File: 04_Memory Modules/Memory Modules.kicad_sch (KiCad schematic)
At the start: 5 parts, among them J1 Data bus, J2 Address bus 1, J3 Address bus 2, J4 Input 1, J5 Input 2

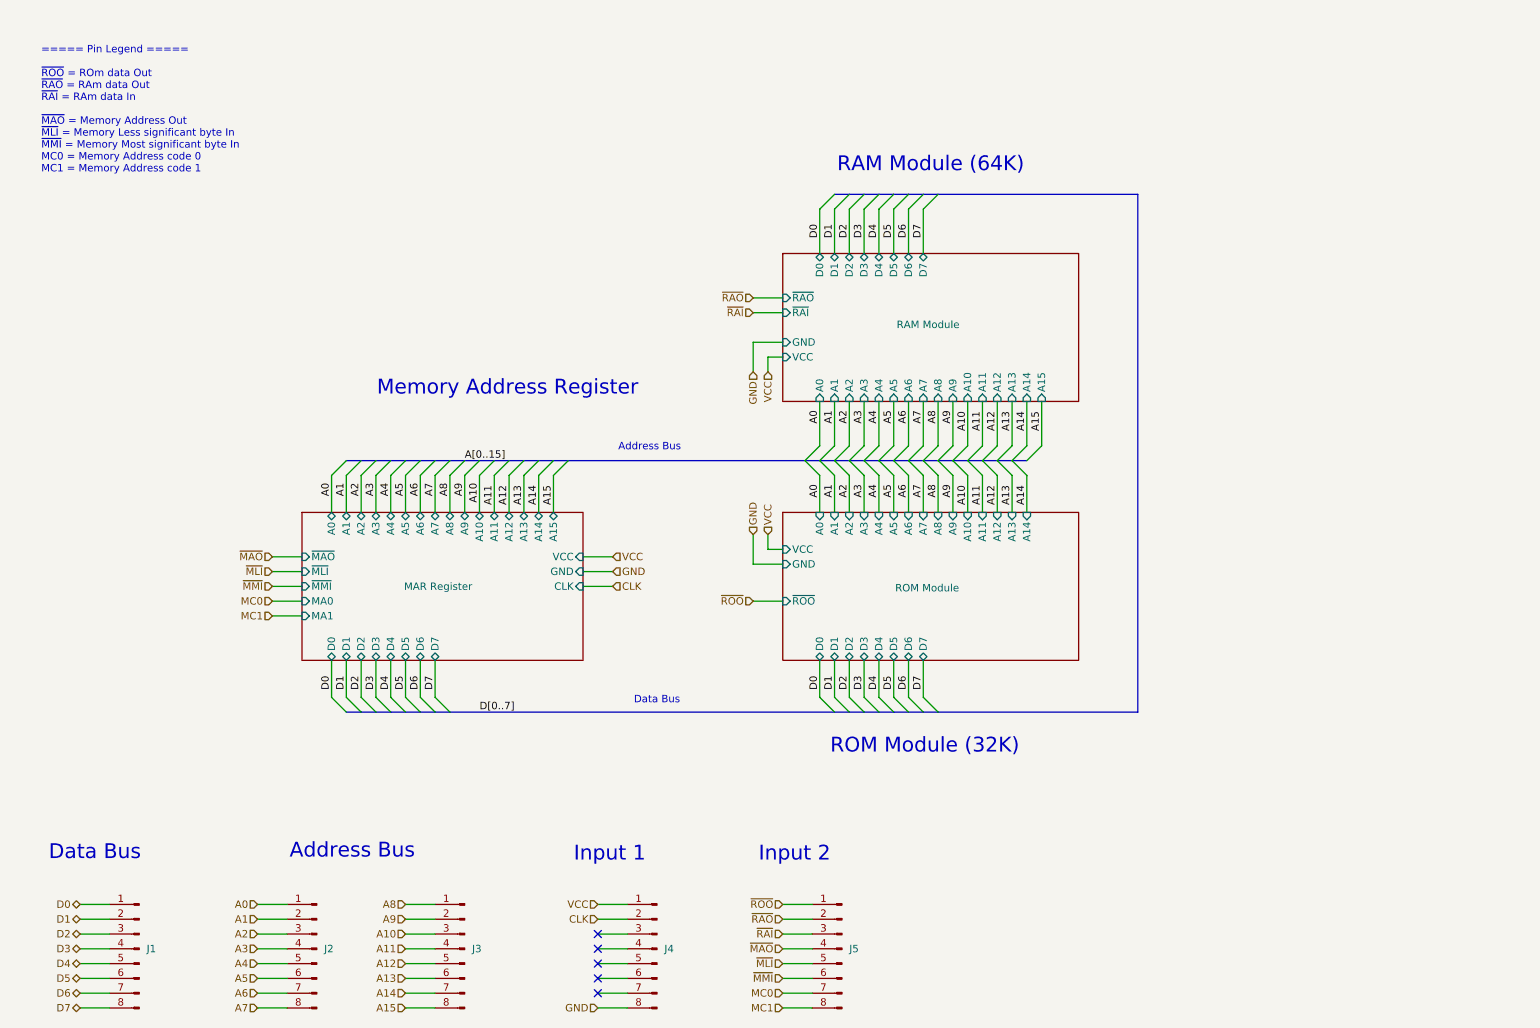
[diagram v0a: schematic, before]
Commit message: Last revision of the cpu, all boards have been ordered. Implementation to be tested and documented in following commits.
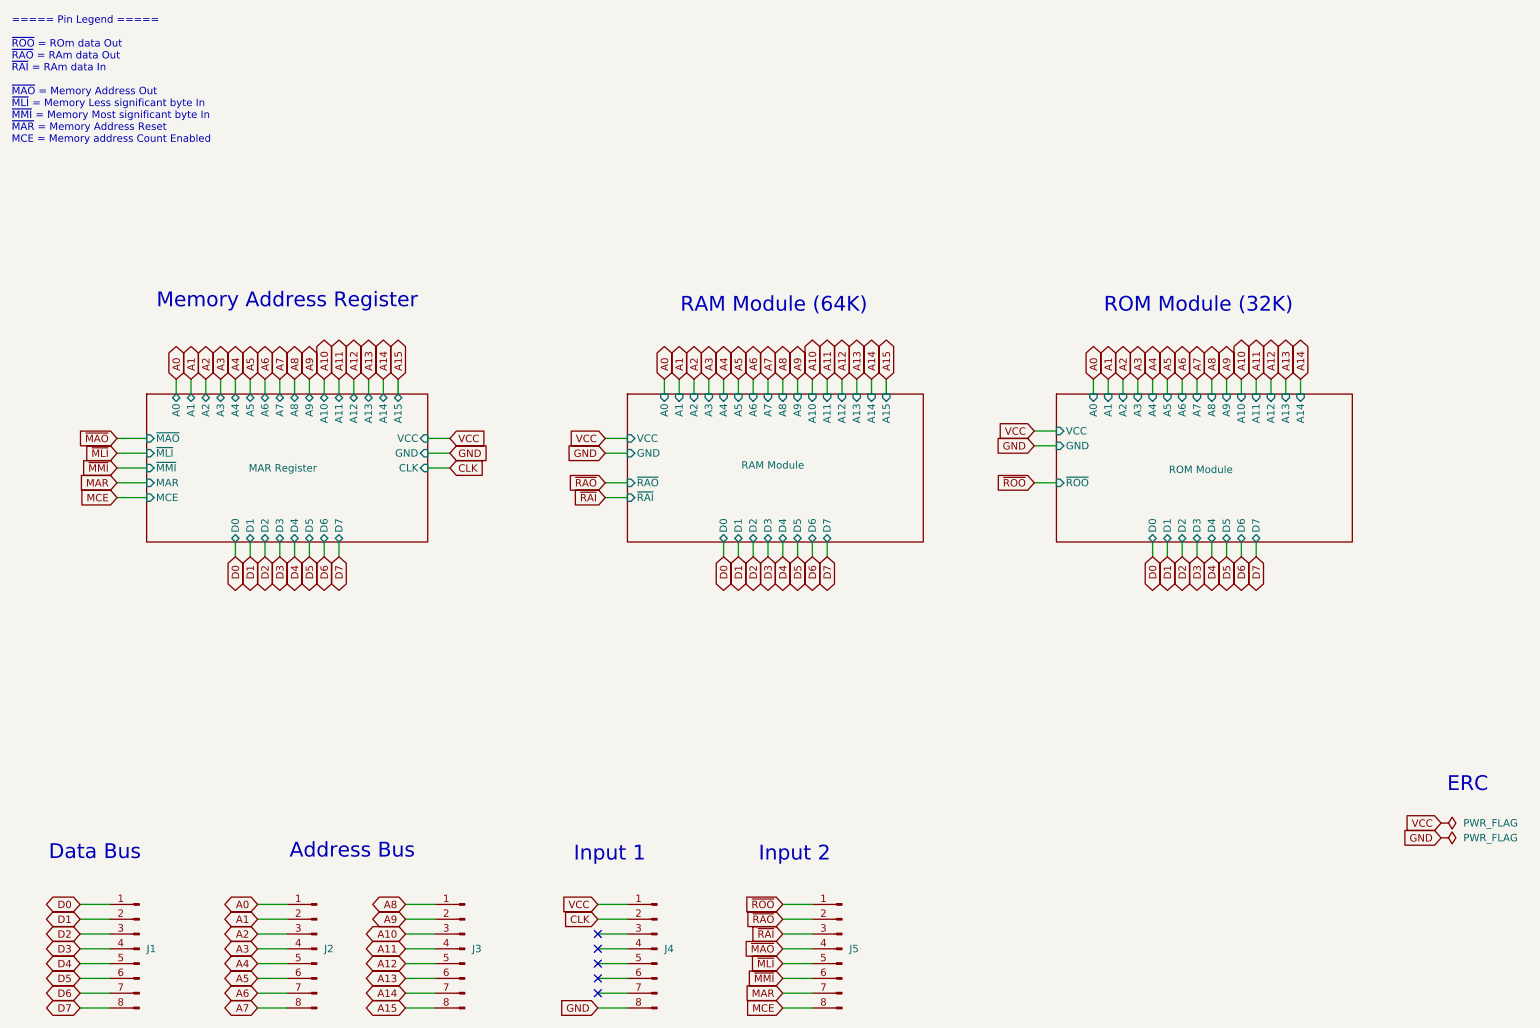
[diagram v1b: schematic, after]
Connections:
- net MC0 renamed MAR
- net MC1 renamed MCE
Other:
- sheet MAR Register ports: added MAR, MCE; removed MA0, MA1
- note added: "ERC"

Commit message: Update 10-01-2026 - Fixed bug on program counter - Fist ISA review, still in draft - Added missing mounting holes on memory modules
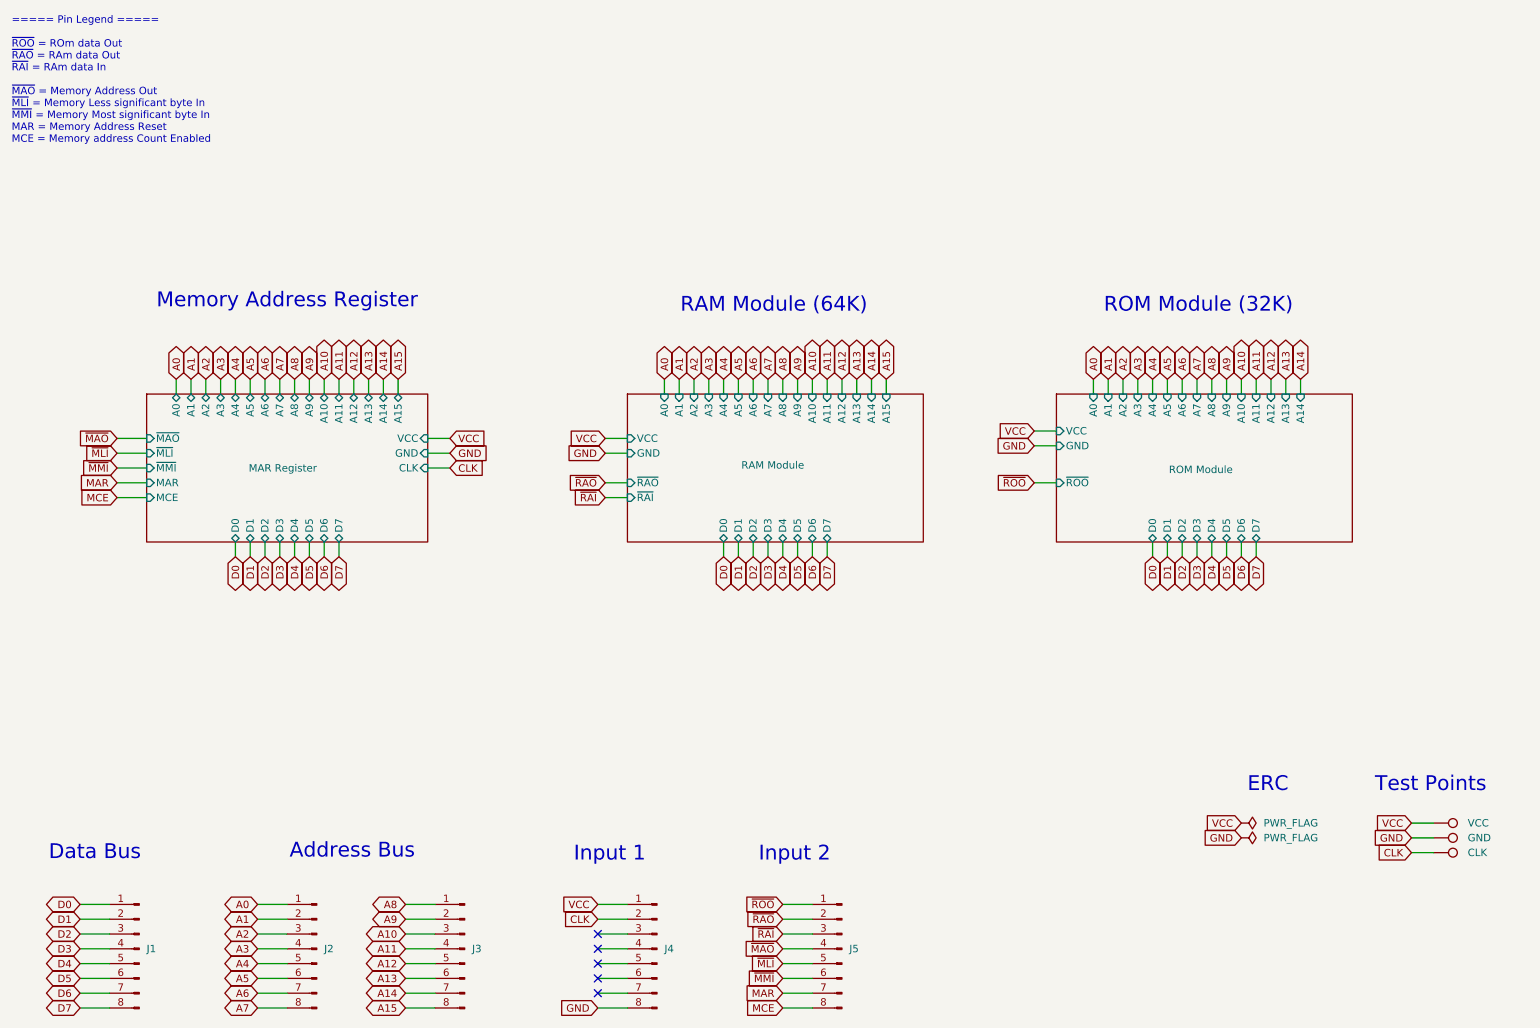
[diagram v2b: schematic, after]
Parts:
- added TP1: GND, TestPoint:TestPoint_Loop_D3.50mm_Drill0.9mm_Beaded, symbol Connector:TestPoint
- added TP2: VCC, TestPoint:TestPoint_Loop_D3.50mm_Drill0.9mm_Beaded, symbol Connector:TestPoint
- added TP3: CLK, TestPoint:TestPoint_Loop_D3.50mm_Drill0.9mm_Beaded, symbol Connector:TestPoint
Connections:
- net CLK: now also TP3.1
- net GND: now also TP1.1
- net VCC: now also TP2.1
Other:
- note added: "Test Points"
